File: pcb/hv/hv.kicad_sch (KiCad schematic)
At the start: 40 parts, among them Q1 IRL540N, Q151 TN2106N3-G, T1 DA2032-AL, U5 LM5155

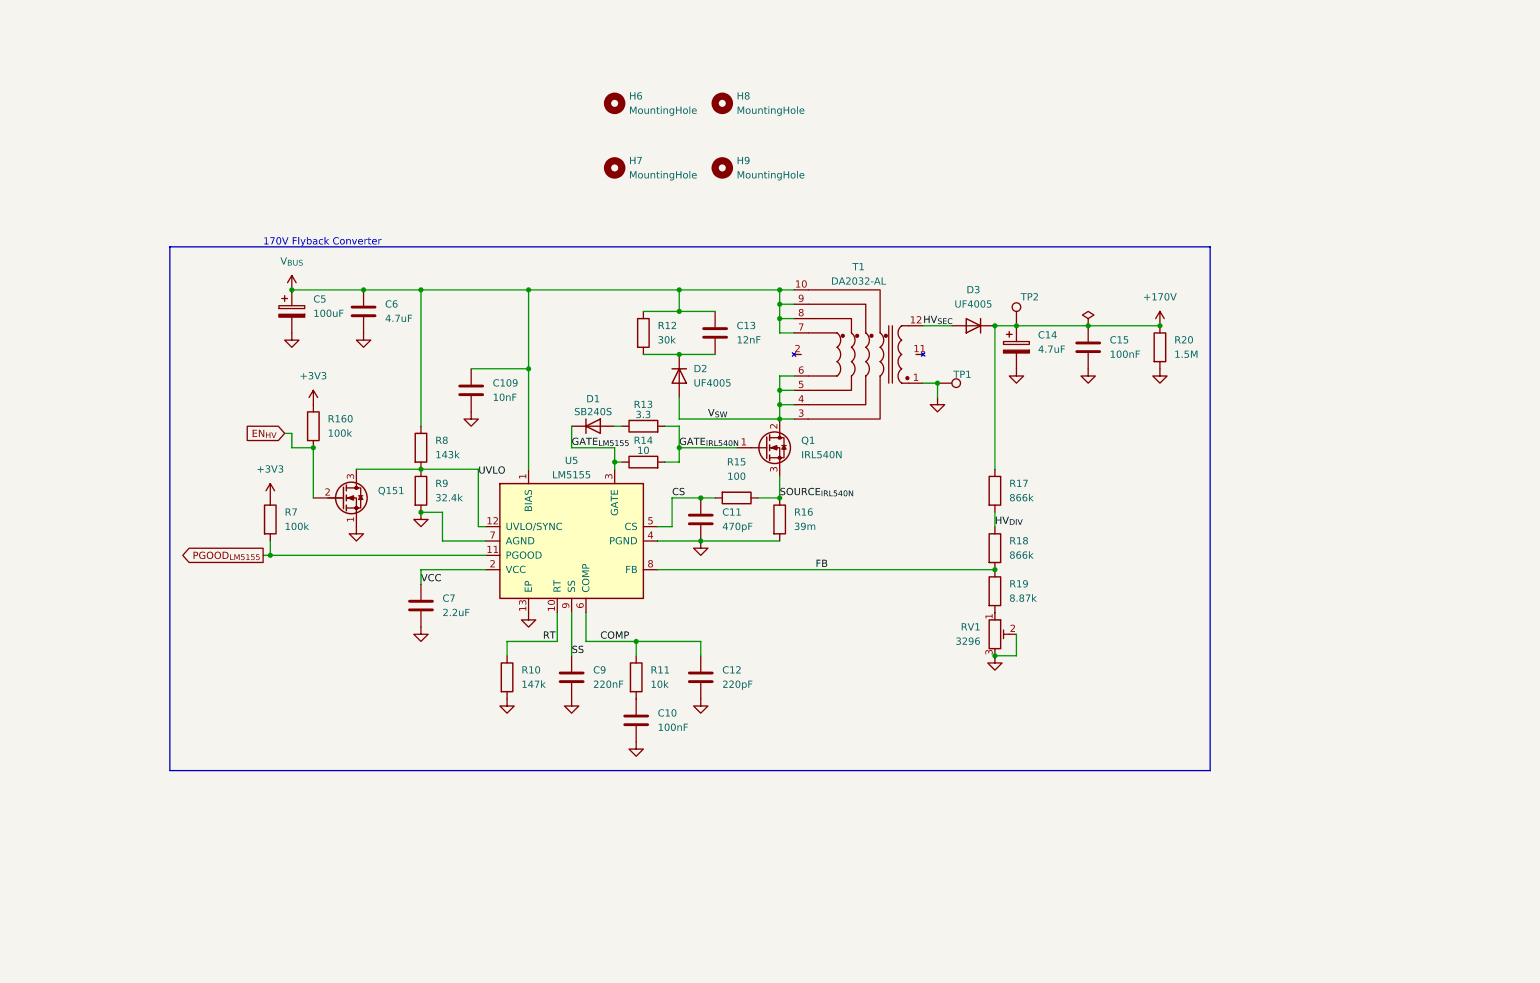
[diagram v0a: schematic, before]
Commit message: Split project into 3
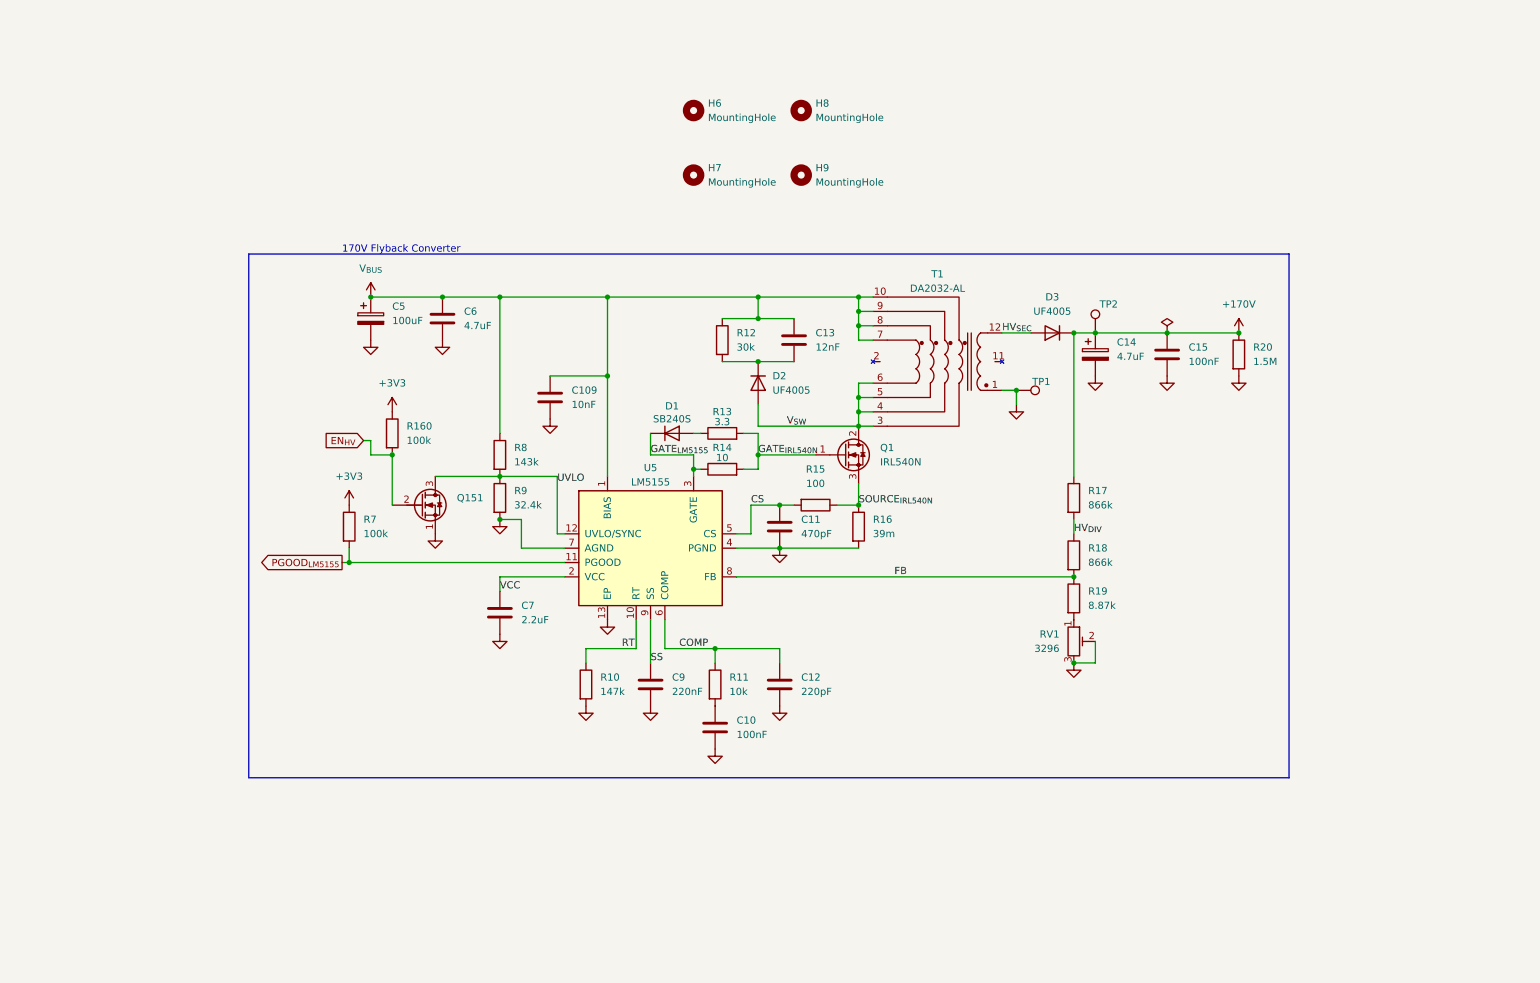
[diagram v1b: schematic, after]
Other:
- title: ${TITLE} -> (none)
- moved on the sheet: C10, C109, C11, C12, C13, C14, C15, C5, C6, C7, C9, D1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

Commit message: Rev B RC1
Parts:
- added J1: JST XH, Connector_JST:JST_XH_S6B-XH-A_1x06_P2.50mm_Horizontal, symbol Connector_Generic:Conn_01x06
- added J2: Phoenix MSTB, Connector_Phoenix_MSTB:PhoenixContact_MSTBA_2,5_3-G-5,08_1x03_P5.08mm_Horizontal, symbol Connector_Generic:Conn_01x03
- renumbered C5 to C1, C12 to C10, C10 to C11, C6 to C2, C13 to C3, C14 to C4, C15 to C5, C109 to C6, C11 to C7, C7 to C8, D3 to D1, D1 to D3, H6 to H1, H8 to H2, H7 to H3, H9 to H4, Q151 to Q2, R12 to R1, R7 to R10, R16 to R11, R18 to R12, R19 to R13, R10 to R14, R11 to R15, R20 to R2, R160 to R3, R13 to R4, R8 to R5, R14 to R6, R9 to R7, R17 to R8, R15 to R9, TP2 to TP1, TP1 to TP2, U5 to U1
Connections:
- net +170V: now also J2.1 (Pin_1)
- net +3V3: now also J1.1 (Pin_1)
- net EN_{HV}: now also J1.2 (Pin_2)
- net GND: now also J1.6 (Pin_6), J2.3 (Pin_3)
- net PGOOD_{LM5155}: now also J1.5 (Pin_5)
- net V_{BUS}: now also J1.3 (Pin_3), J1.4 (Pin_4)
- no-connect marks 0 -> 1

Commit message: Final Rev B
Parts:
- J1, J2: now left out of the parts list
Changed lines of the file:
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@@
 		(unit 1)
 		(exclude_from_sim no)
-		(in_bom yes)
+		(in_bom no)
 		(on_board yes)
 		(dnp no)
@@
 		(unit 1)
 		(exclude_from_sim no)
-		(in_bom yes)
+		(in_bom no)
 		(on_board yes)
 		(dnp no)

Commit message: HV converter Rev C redesign around LM5156
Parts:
- removed U1: LM5155, nixie_clock:WSON-12-1EP_3x2mm_P0.5mm_EP1x2.65_ThermalVias, symbol nixie_clock:LM5155
- added C12: 4.7nF, C0G, 0_nixie_clock:C_Rect_L3.8mm_W2.5mm_P2.54mm_Goldmax, symbol Device:C
- added D4: ZPD3B0, Diode_THT:D_DO-35_SOD27_P7.62mm_Horizontal, symbol Device:D_Zener
- added D5: SB140-T, Diode_THT:D_DO-41_SOD81_P7.62mm_Horizontal, symbol Device:D_Schottky
- added D6, D7: 1N4148, Diode_THT:D_DO-35_SOD27_P7.62mm_Horizontal, symbol Device:D
- added R16: 82, Resistor_THT:R_Axial_DIN0309_L9.0mm_D3.2mm_P12.70mm_Horizontal, symbol Device:R
- added U1: LM5156H, 0_nixie_clock:Texas_HTSSOP-14-1EP_4.4x5mm_P0.65mm_EP3.4x5mm_Mask3.155x3.255mm_ThermalVias, symbol 0_nixie_clock:LM5156H
- C1, C4: footprint Capacitor_THT:CP_Radial_D8.0mm_P3.50mm -> 0_nixie_clock:CP_Radial_D8.0mm_P3.50mm
- C10: value 220pF -> 220pF, C0G; footprint nixie_clock:C_Rect_L5.1mm_W3.2mm_P5.08mm_Goldmax -> 0_nixie_clock:C_Rect_L5.1mm_W3.2mm_P5.08mm_Goldmax; MFG Part No C322C221K5R5TA -> C322C221J2G5TA
- C11, C2: footprint nixie_clock:C_Rect_L5.1mm_W3.2mm_P5.08mm_Goldmax -> 0_nixie_clock:C_Rect_L5.1mm_W3.2mm_P5.08mm_Goldmax
- C3: footprint nixie_clock:C_Rect_L3.8mm_W2.5mm_P5.08mm_Goldmax -> 0_nixie_clock:C_Rect_L7.2mm_W2.5mm_P5.00mm_PHE426; MFG Part No C317C123K1R5TA7301 -> PHE426DJ5120JR05
- C5: footprint nixie_clock:C_Rect_L7.9mm_W5.9mm_P5.00mm_ECQE -> 0_nixie_clock:C_Rect_L7.9mm_W5.9mm_P5.00mm_ECQE
- C6: value 10nF -> 1uF; footprint nixie_clock:C_Rect_L5.1mm_W3.2mm_P5.08mm_Goldmax -> 0_nixie_clock:C_Rect_L7.1mm_W4.1mm_P5.08mm_Goldmax; MFG Part No C322C103K5R5TA -> C330C105K5R5TA7303
- C7: value 470pF -> 470pF, C0G; footprint nixie_clock:C_Rect_L3.8mm_W2.5mm_P2.54mm_Goldmax -> 0_nixie_clock:C_Rect_L3.8mm_W2.5mm_P2.54mm_Goldmax; MFG Part No C315C471K5R5TA -> C315C471J1G5TA
- C8: footprint nixie_clock:C_Rect_L5.1mm_W3.2mm_P5.08mm_Goldmax -> Capacitor_THT:C_Axial_L5.1mm_D3.1mm_P7.50mm_Horizontal; MFG Part No C322C225K5R5TA -> C410C225K3R5TA
- C9: value 220nF -> 470nF; footprint nixie_clock:C_Rect_L5.1mm_W3.2mm_P5.08mm_Goldmax -> 0_nixie_clock:C_Rect_L5.1mm_W3.2mm_P5.08mm_Goldmax; MFG Part No C322C224K5R5TA7301 -> C322C474K5R5TA7301
- R1: renamed from R2; footprint Resistor_THT:R_Axial_DIN0207_L6.3mm_D2.5mm_P7.62mm_Horizontal -> Resistor_THT:R_Axial_DIN0309_L9.0mm_D3.2mm_P12.70mm_Horizontal; MFG Part No MFR-25FBF52-1M5 -> CFR-50JB-52-1M5
- R10: footprint Resistor_THT:R_Axial_DIN0207_L6.3mm_D2.5mm_P7.62mm_Horizontal -> Resistor_THT:R_Axial_DIN0204_L3.6mm_D1.6mm_P5.08mm_Horizontal; MFG Part No MFR-25FRF52-100K -> CFR-12JB-52-100K
- R11: renamed from R8; value 866k -> 845k; MFG Part No MFR-25FRF52-866K -> MFR-25FBF52-845K
- R12: value 866k -> 845k; MFG Part No MFR-25FRF52-866K -> MFR-25FBF52-845K
- R13: value 8.87k -> 8.25k; MFG Part No MFR-25FBF52-8K87 -> MFR-25FBF52-8K25
- R15: footprint Resistor_THT:R_Axial_DIN0207_L6.3mm_D2.5mm_P7.62mm_Horizontal -> Resistor_THT:R_Axial_DIN0204_L3.6mm_D1.6mm_P5.08mm_Horizontal; MFG Part No MFR-25FRF52-10K -> CFR-12JB-52-10K
- R2: renamed from R3; footprint Resistor_THT:R_Axial_DIN0207_L6.3mm_D2.5mm_P7.62mm_Horizontal -> Resistor_THT:R_Axial_DIN0204_L3.6mm_D1.6mm_P5.08mm_Horizontal; MFG Part No MFR-25FRF52-100K -> CFR-12JB-52-100K
- R3: renamed from R1; MFG Part No MFR-25FRF52-30K -> CFR-25JB-52-30K
- R4: footprint Resistor_THT:R_Axial_DIN0207_L6.3mm_D2.5mm_P7.62mm_Horizontal -> Resistor_THT:R_Axial_DIN0204_L3.6mm_D1.6mm_P5.08mm_Horizontal; MFG Part No MFR-25FTE52-3R3 -> CFR-12JB-52-3R3
- R5: renamed from R6; footprint Resistor_THT:R_Axial_DIN0207_L6.3mm_D2.5mm_P7.62mm_Horizontal -> Resistor_THT:R_Axial_DIN0204_L3.6mm_D1.6mm_P5.08mm_Horizontal; MFG Part No MFR-25FBF52-10R -> CFR25SJT-52-10R
- R6: renamed from R5; value 143k -> 63.4k; MFG Part No MFR-25FRF52-143K -> MFR-25FRF52-63K4
- R9: footprint Resistor_THT:R_Axial_DIN0207_L6.3mm_D2.5mm_P7.62mm_Horizontal -> Resistor_THT:R_Axial_DIN0204_L3.6mm_D1.6mm_P5.08mm_Horizontal; MFG Part No MFR-25FBF52-100R -> CFR25SJT-52-100R
- T1: footprint nixie_clock:DA2032-AL -> 0_nixie_clock:DA2032-AL; symbol nixie_clock:DA2032-AL -> 0_nixie_clock:DA2032-AL
- renumbered R11 to R8
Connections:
- net COMP: now also U1.8 (COMP)
- net CS: now also U1.7 (CS)
- net FB: now also U1.10 (FB)
- net GND: now also D4.2 (A), D7.2 (A), U1.15 (EP), U1.5 (PGND), U1.6 (AGND)
- net RT: now also U1.12 (RT)
- net SS: now also U1.11 (SS)
- net UVLO: now also U1.14 (EN/UVLO/SYNC)
- net VCC: now also U1.3 (VCC), U1.9 (DITHOFF)
- net V_{BUS}: now also D5.2 (A); no longer C6.2
- net V_{SW}: now also C12.1
- net SW_{CLAMP}: now reaches C3.1, D2.1 (K), R3.2
- net EN_{HV} renamed ~{EN}_{HV}
- net GATE_{IRL540N} renamed GATE_{2}
- net GATE_{LM5155} renamed GATE_{1}
- net GATE_{1}: now also U1.4 (GATE)
- net PGOOD_{LM5155} renamed PGOOD_{HV}
- net PGOOD_{HV}: now also U1.13 (PGOOD)
- net SOURCE_{IRL540N} renamed SOURCE_{SW}
- new net: C12.2, R16.1
- new net BIAS: C6.2, D4.1 (K), D5.1 (K), D6.1 (K), U1.1 (BIAS)
- new net SW_{PUMP}: D6.2 (A), D7.1 (K), R16.2
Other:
- note added: "Bias Charge Pump"
- note added: "RCD Clamp"
- note added: "To Clock Face"
- note added: "To Main Board"
- moved on the sheet: C1, C10, C11, C2, C3, C4, C5, C6, C7, C8, C9, D1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

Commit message: Fix ballast/divider resistors to match first line of table 5-2
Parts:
- R13: value 8.25k -> 9.09k; MFG Part No MFR-25FBF52-8K25 -> MFR-25FBF52-9k09
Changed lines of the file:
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@@
 			)
 		)
-		(property "Value" "8.25k"
+		(property "Value" "9.09k"
 			(at 165.1 80.0099 0)
 			(show_name no)
@@
 			)
 		)
-		(property "MFG Part No" "MFR-25FBF52-8K25"
+		(property "MFG Part No" "MFR-25FBF52-9k09"
 			(at 162.56 78.74 0)
 			(hide yes)

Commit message: Fix part number on hv divider resistor
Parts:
- R13: MFG Part No MFR-25FBF52-9k09 -> MFR-25FBF52-9K09
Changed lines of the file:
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@@
 			)
 		)
-		(property "MFG Part No" "MFR-25FBF52-9k09"
+		(property "MFG Part No" "MFR-25FBF52-9K09"
 			(at 162.56 78.74 0)
 			(hide yes)

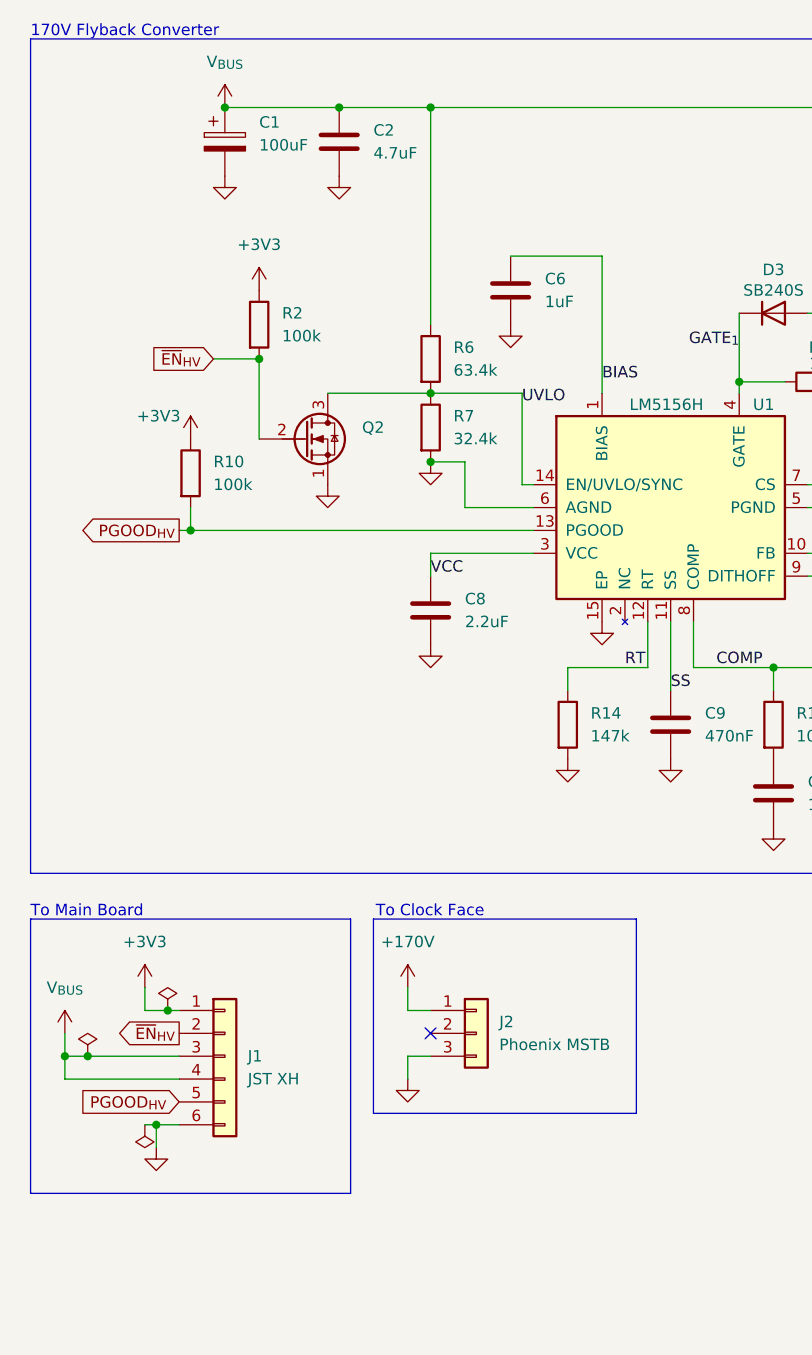
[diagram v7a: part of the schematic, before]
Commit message: Update ins1 tube model, update hv/main connector to 1 vbus, 2 gnd connections, update hv inhibit circuit to be default inhibit and require positive enable from MCU
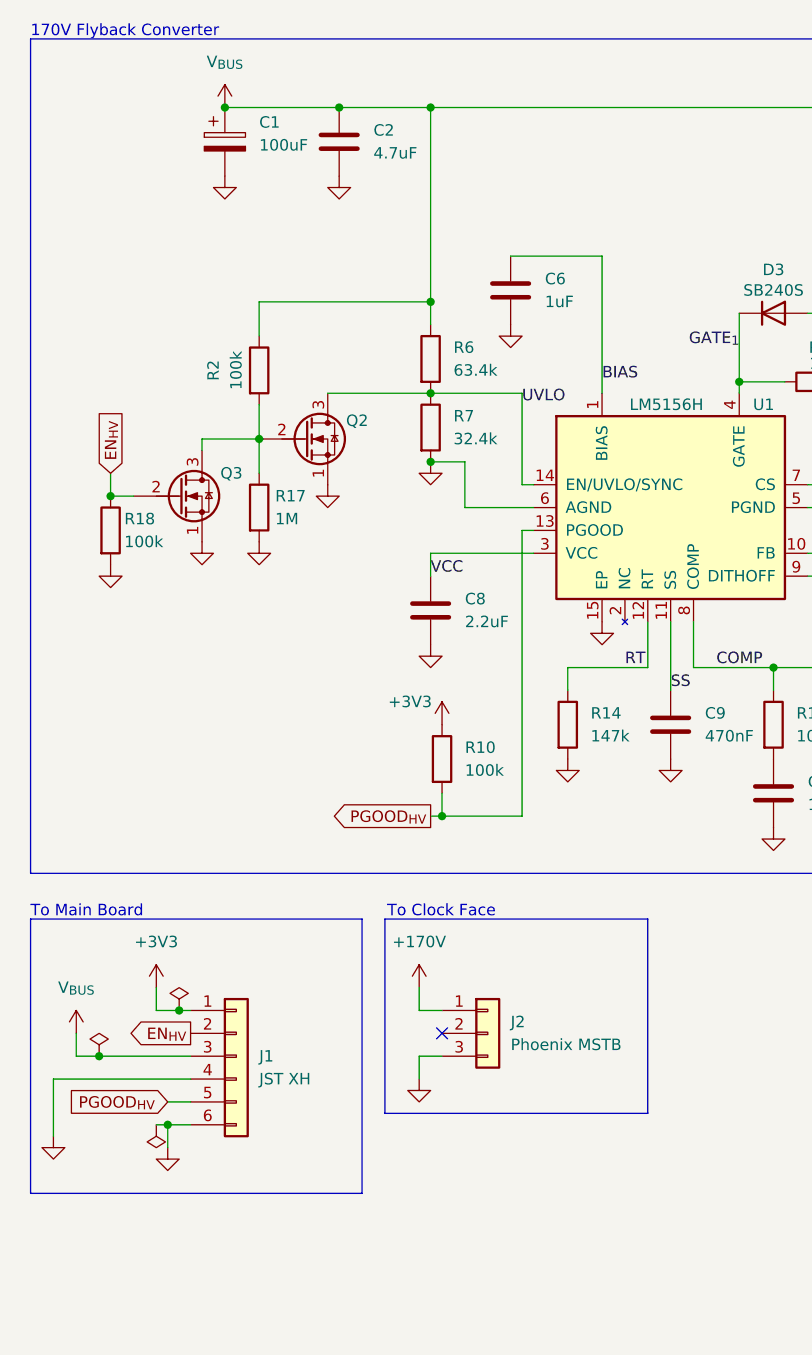
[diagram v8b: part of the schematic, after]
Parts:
- added Q3: TN2106N3-G, Package_TO_SOT_THT:TO-92L, symbol Transistor_FET:Q_NMOS_SGD
- added R17: 1M, Resistor_THT:R_Axial_DIN0204_L3.6mm_D1.6mm_P5.08mm_Horizontal, symbol Device:R
- added R18: 100k, Resistor_THT:R_Axial_DIN0204_L3.6mm_D1.6mm_P5.08mm_Horizontal, symbol Device:R
- J1: MFG Part No (none) -> S6B-XH-A; now in the parts list
- J2: now in the parts list
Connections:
- net +3V3: no longer R2.1
- net GND: now also J1.4 (Pin_4), Q3.1 (S), R17.2, R18.2
- net V_{BUS}: now also R2.1; no longer J1.4 (Pin_4)
- net ~{EN}_{HV}: no longer names the net of Q2.2 (G), R2.2
- net ~{EN}_{HV}: now also Q3.3 (D), R17.1; no longer J1.2 (Pin_2)
- new net EN_{HV}: J1.2 (Pin_2), Q3.2 (G), R18.1
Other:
- moved on the sheet: J1, J2, R10, R2
